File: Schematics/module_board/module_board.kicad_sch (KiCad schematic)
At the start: 2 parts, among them J1 Conn_01x06_Male

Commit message: Added
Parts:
- added C?: C, symbol Device:C
- added J?: Conn_01x06_Male, symbol Connector:Conn_01x06_Male
- added R?: R, symbol Device:R
- added SW?: SW_Push, symbol Switch:SW_Push
- added U?: LSM6DS3, Package_LGA:LGA-14_3x2.5mm_P0.5mm_LayoutBorder3x4y, symbol Sensor_Motion:LSM6DS3
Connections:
- net +3V3: now also R?.1
- net GND: now also C?.1, J?.2 (Pin_2), SW?.2, U?.4 (INT1), U?.6 (GND), U?.7 (GND), U?.9 (INT2)
- new net +3.3V: C?.2, J?.1 (Pin_1), U?.2 (SDX), U?.3 (SCX), U?.5 (VDDIO), U?.8 (VDD)
- new net ACC_CLK: J?.4 (Pin_4), U?.13 (SCL)
- new net ACC_CS: J?.3 (Pin_3), U?.12 (CS)
- new net ACC_RX: J?.5 (Pin_5), U?.14 (SDA)
- new net ACC_TX: J?.6 (Pin_6), U?.1 (SDO/SA0)
- new net RESET: R?.2, SW?.1
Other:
- note added: "Accelerometer/Gyroscope Component"
- note added: "Toggleable Switch Component"
- moved on the sheet: J1, SWD1

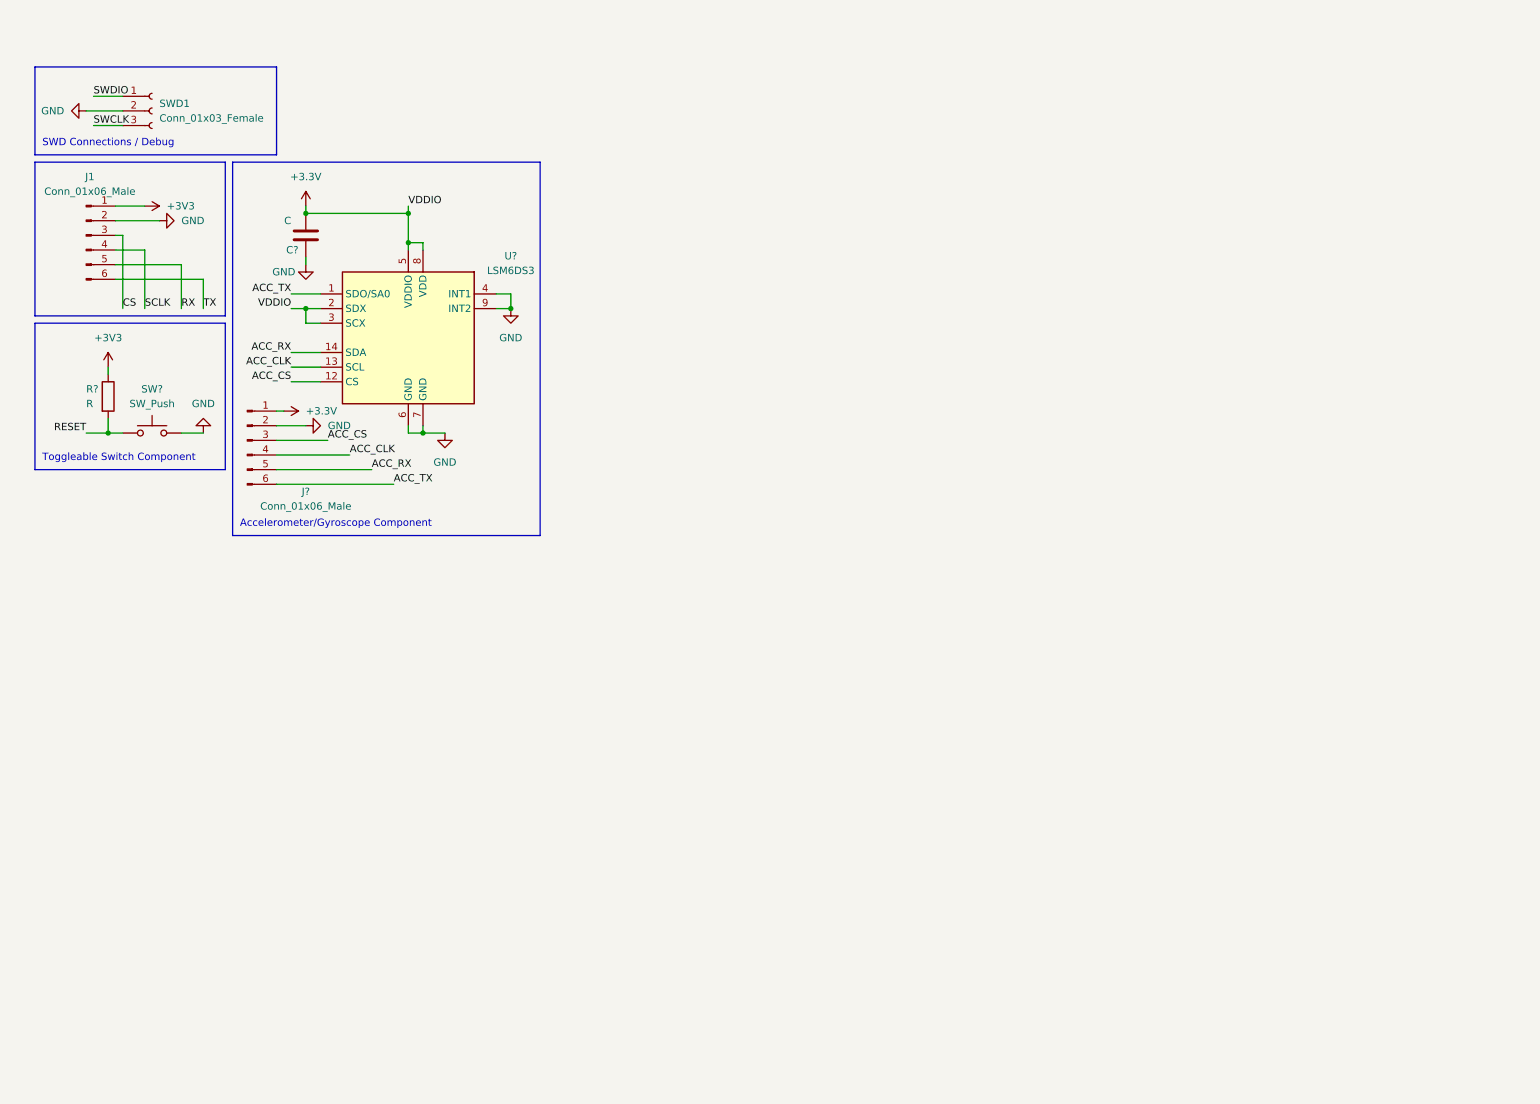
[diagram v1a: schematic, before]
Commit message: Add MCU to module board schematic
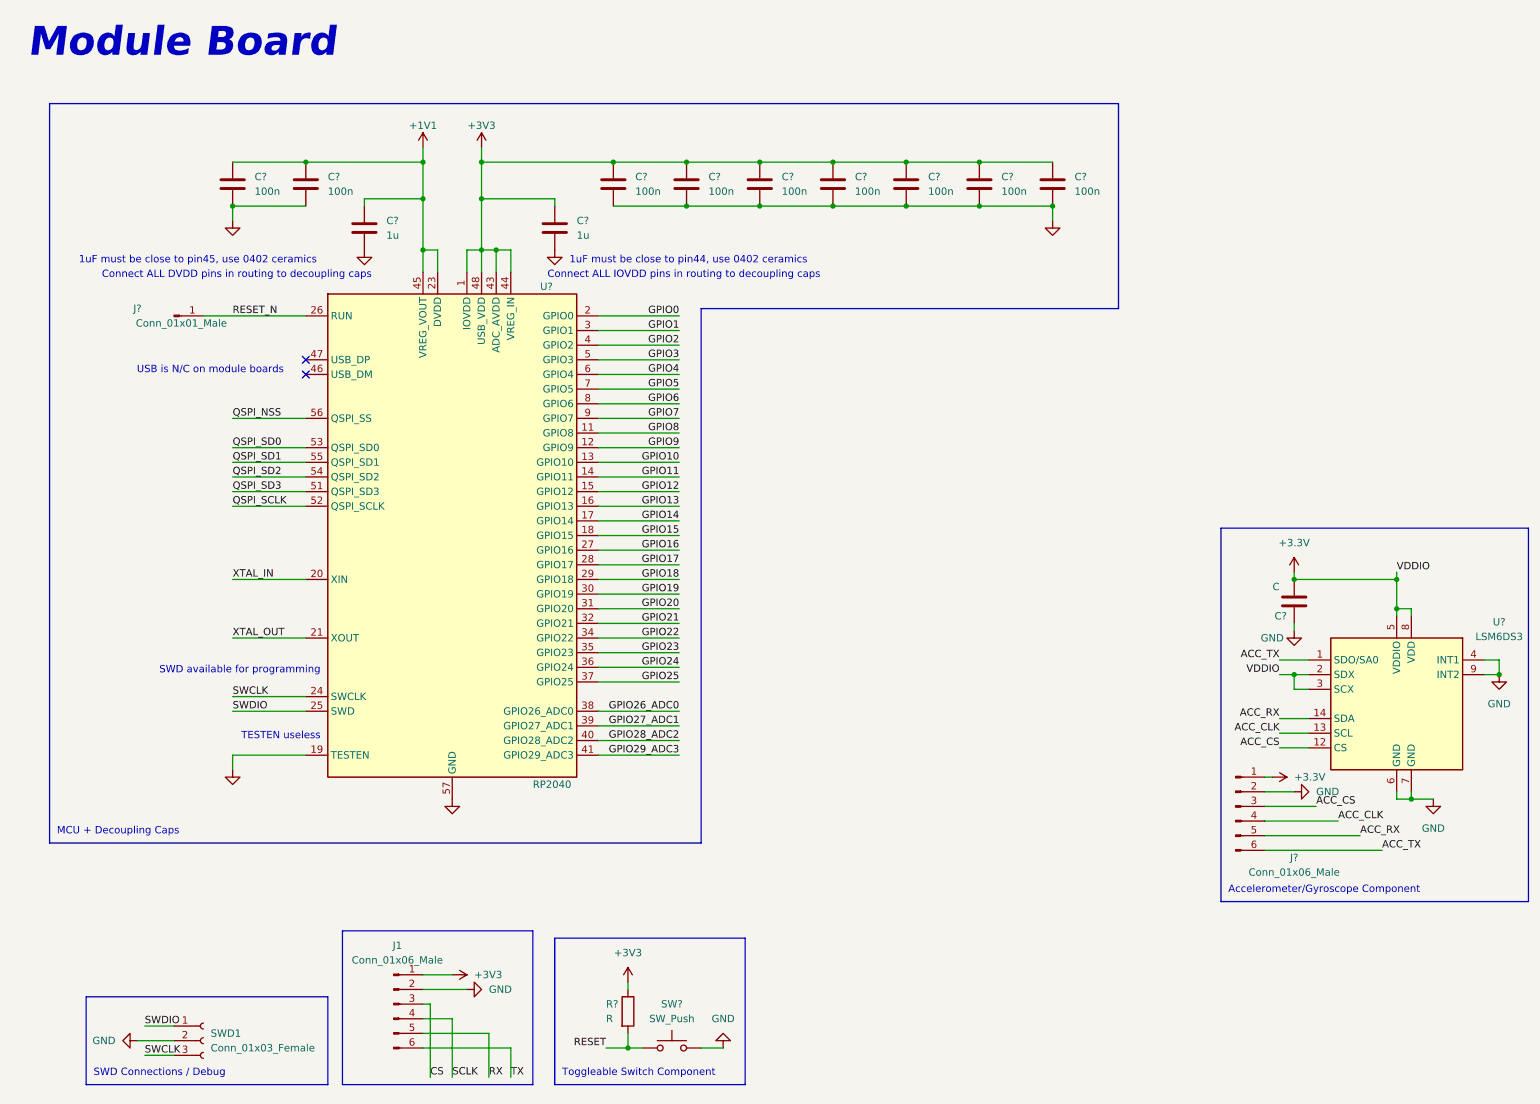
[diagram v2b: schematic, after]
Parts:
- added C? (x9): 100n, symbol Device:C
- added C? (x2): 1u, symbol Device:C
- added J?: Conn_01x01_Male, symbol Connector:Conn_01x01_Male
- added U?: RP2040, Package_DFN_QFN:QFN-56-1EP_7x7mm_P0.4mm_EP3.2x3.2mm, symbol MCU_RaspberryPi:RP2040
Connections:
- net +3V3: now also C?.1, C?.1, C?.1, C?.1, C?.1, C?.1, C?.1, C?.1, U?.1 (IOVDD), U?.10 (IOVDD), U?.22 (IOVDD), U?.33 (IOVDD), U?.42 (IOVDD), U?.43 (ADC_AVDD), U?.44 (VREG_IN), U?.48 (USB_VDD), U?.49 (IOVDD)
- net GND: now also C?.2, C?.2, C?.2, C?.2, C?.2, C?.2, C?.2, C?.2, C?.2, C?.2, C?.2, U?.19 (TESTEN), U?.57 (GND)
- net SWCLK: now also U?.24 (SWCLK)
- net SWDIO: now also U?.25 (SWD)
- new net +1V1: C?.1, C?.1, C?.1, U?.23 (DVDD), U?.45 (VREG_VOUT), U?.50 (DVDD)
- new net GPIO0: U?.2 (GPIO0)
- new net GPIO1: U?.3 (GPIO1)
- new net GPIO10: U?.13 (GPIO10)
- new net GPIO11: U?.14 (GPIO11)
- new net GPIO12: U?.15 (GPIO12)
- new net GPIO13: U?.16 (GPIO13)
- new net GPIO14: U?.17 (GPIO14)
- new net GPIO15: U?.18 (GPIO15)
- new net GPIO16: U?.27 (GPIO16)
- new net GPIO17: U?.28 (GPIO17)
- new net GPIO18: U?.29 (GPIO18)
- new net GPIO19: U?.30 (GPIO19)
- new net GPIO2: U?.4 (GPIO2)
- new net GPIO20: U?.31 (GPIO20)
- new net GPIO21: U?.32 (GPIO21)
- new net GPIO22: U?.34 (GPIO22)
- new net GPIO23: U?.35 (GPIO23)
- new net GPIO24: U?.36 (GPIO24)
- new net GPIO25: U?.37 (GPIO25)
- new net GPIO26_ADC0: U?.38 (GPIO26_ADC0)
- new net GPIO27_ADC1: U?.39 (GPIO27_ADC1)
- new net GPIO28_ADC2: U?.40 (GPIO28_ADC2)
- new net GPIO29_ADC3: U?.41 (GPIO29_ADC3)
- new net GPIO3: U?.5 (GPIO3)
- new net GPIO4: U?.6 (GPIO4)
- new net GPIO5: U?.7 (GPIO5)
- new net GPIO6: U?.8 (GPIO6)
- new net GPIO7: U?.9 (GPIO7)
- new net GPIO8: U?.11 (GPIO8)
- new net GPIO9: U?.12 (GPIO9)
- new net QSPI_NSS: U?.56 (QSPI_SS)
- new net QSPI_SCLK: U?.52 (QSPI_SCLK)
- new net QSPI_SD0: U?.53 (QSPI_SD0)
- new net QSPI_SD1: U?.55 (QSPI_SD1)
- new net QSPI_SD2: U?.54 (QSPI_SD2)
- new net QSPI_SD3: U?.51 (QSPI_SD3)
- new net RESET_N: J?.1 (Pin_1), U?.26 (RUN)
- new net XTAL_IN: U?.20 (XIN)
- new net XTAL_OUT: U?.21 (XOUT)
- no-connect marks 0 -> 2
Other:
- note added: "1uF must be close to pin44, use 0402 ceramics"
- note added: "1uF must be close to pin45, use 0402 ceramics"
- note added: "Connect ALL DVDD pins in routing to decoupling caps"
- note added: "Connect ALL IOVDD pins in routing to decoupling caps"
- note added: "MCU + Decoupling Caps"
- note added: "Module Board"
- note added: "SWD available for programming"
- note added: "TESTEN useless"
- note added: "USB is N/C on module boards"
- moved on the sheet: C?, J1, J?, R?, SW?, SWD1, U?

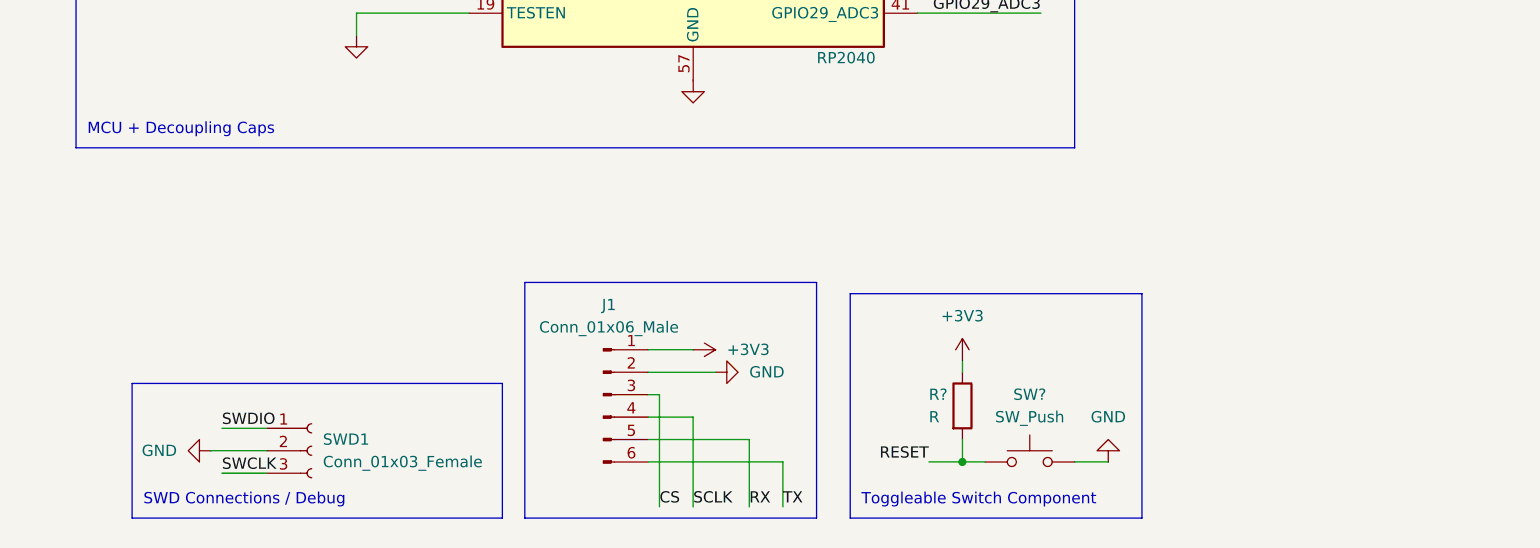
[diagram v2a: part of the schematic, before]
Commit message: Added switch and slider components
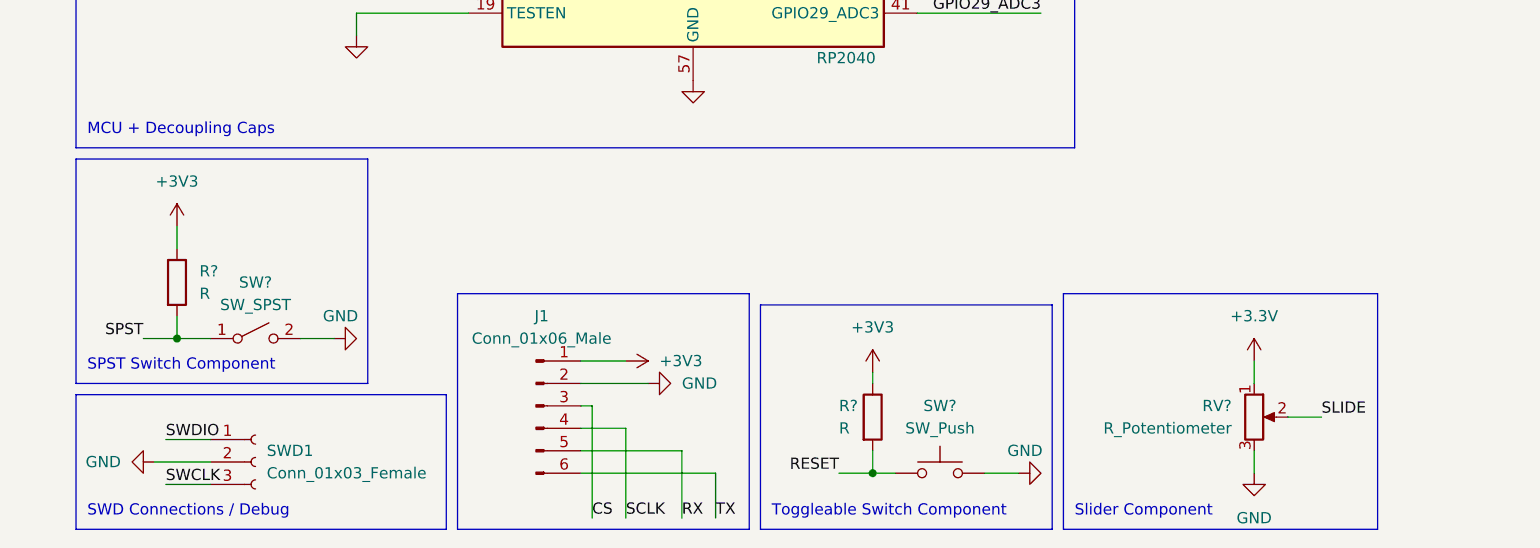
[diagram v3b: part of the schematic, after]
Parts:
- added R?: R, symbol Device:R
- added RV?: R_Potentiometer, symbol Device:R_Potentiometer
- added SW?: SW_SPST, symbol Switch:SW_SPST
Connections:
- net +3.3V: now also RV?.1
- net +3V3: now also R?.1
- net GND: now also RV?.3, SW?.2 (B)
- new net SLIDE: RV?.2
- new net SPST: R?.2, SW?.1 (A)
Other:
- note added: "SPST Switch Component"
- note added: "Slider Component"
- moved on the sheet: J1, R?, SW?, SWD1

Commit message: Consolidated board segments into corresponding board schematic & annotated components
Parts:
- added C10: 100nF, symbol Device:C
- added C7, C8: 10pF, symbol Device:C
- added R3: 1k, symbol Device:R
- added R4: 10k, symbol Device:R
- added U2: W25Q64JVXGIQ, symbol Flash_Memory:W25Q64JVXGIQ
- added Y1: Crystal_GND2, symbol Device:Crystal_GND2
- gave numbers to parts that had none: 21
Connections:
- net +3V3: now also C10.1, R4.1, U2.8 (VCC)
- net GND: now also C10.2, C7.1, C8.1, U2.4 (GND), Y1.2
- new net: C8.2, R3.1, Y1.3
- new net: R4.2, U2.1 (CS_L)
- new net: C7.2, Y1.1
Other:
- note added: "8MB FLASH"
- note added: "Crystal Oscillator"
- note added: "QSPI_CS_L"
- note added: "QSPI_SCLK"
- note added: "QSPI_SD0"
- note added: "QSPI_SD1"
- note added: "QSPI_SD2"
- note added: "QSPI_SD3"
- note added: "TODO: Add SPI Headers for Accelerometer?"
- note added: "XTAL_IN"
- note added: "XTAL_OUT"

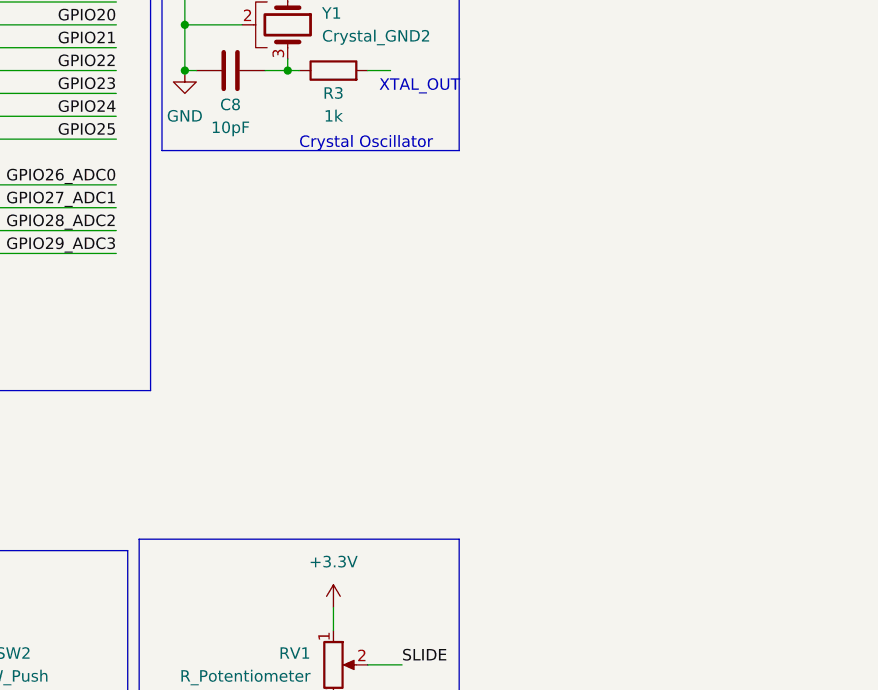
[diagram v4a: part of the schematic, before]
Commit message: Added XYBA Buttons/D-Pad onto module_board.kicad_sch
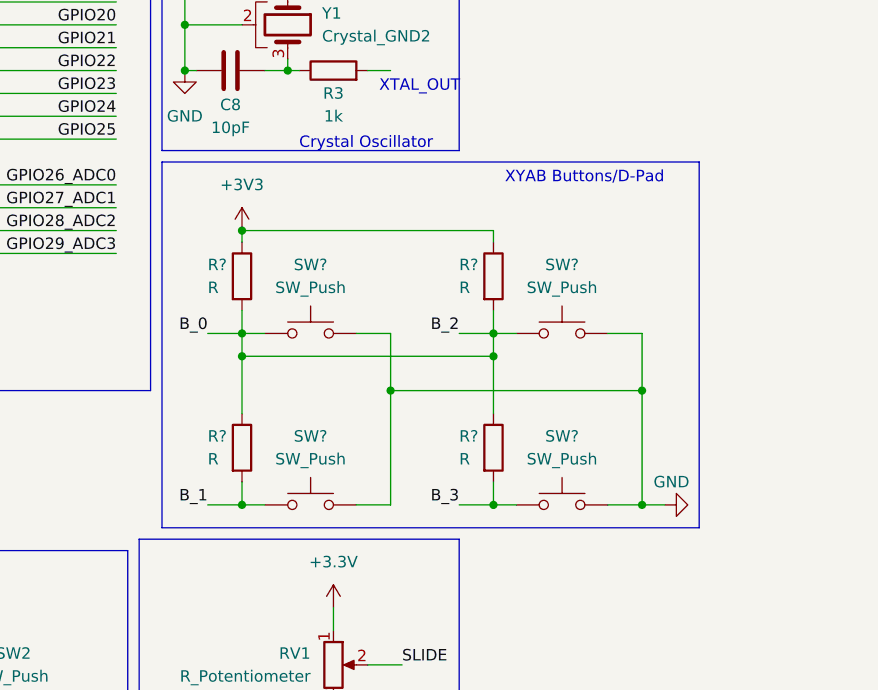
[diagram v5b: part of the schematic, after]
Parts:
- added R? (x4): R, symbol Device:R
- added SW? (x4): SW_Push, symbol Switch:SW_Push
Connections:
- net +3V3: now also R?.1, R?.1
- net GND: now also SW?.2, SW?.2, SW?.2, SW?.2
- new net B_0: R?.1, R?.1, R?.2, R?.2, SW?.1, SW?.1
- new net B_1: R?.2, SW?.1
- new net B_3: R?.2, SW?.1
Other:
- note added: "XYAB Buttons/D-Pad"
